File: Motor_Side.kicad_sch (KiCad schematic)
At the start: 30 parts, among them U2 TLV9301xDCK, U3 TLV9301xDCK, U4 TCMT1106, U5 TCMT1106

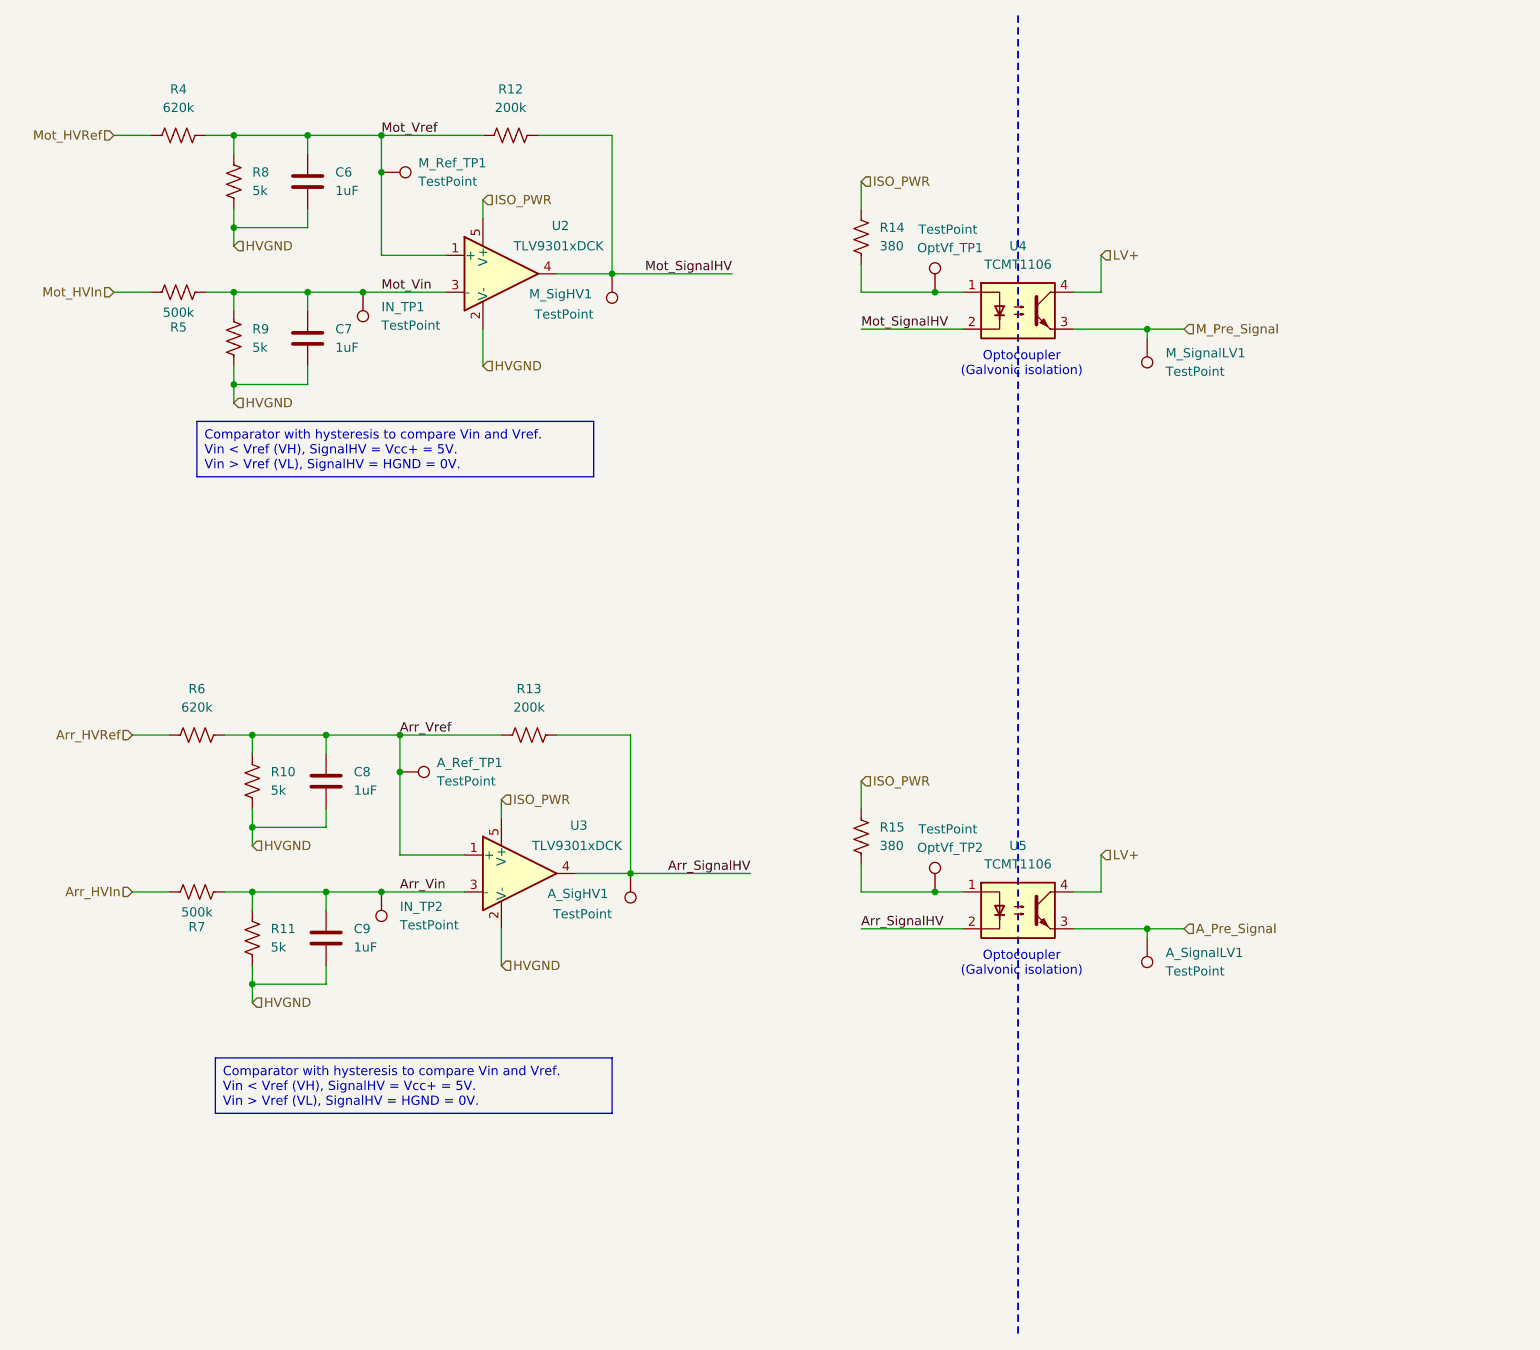
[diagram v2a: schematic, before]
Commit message: started on HV layout
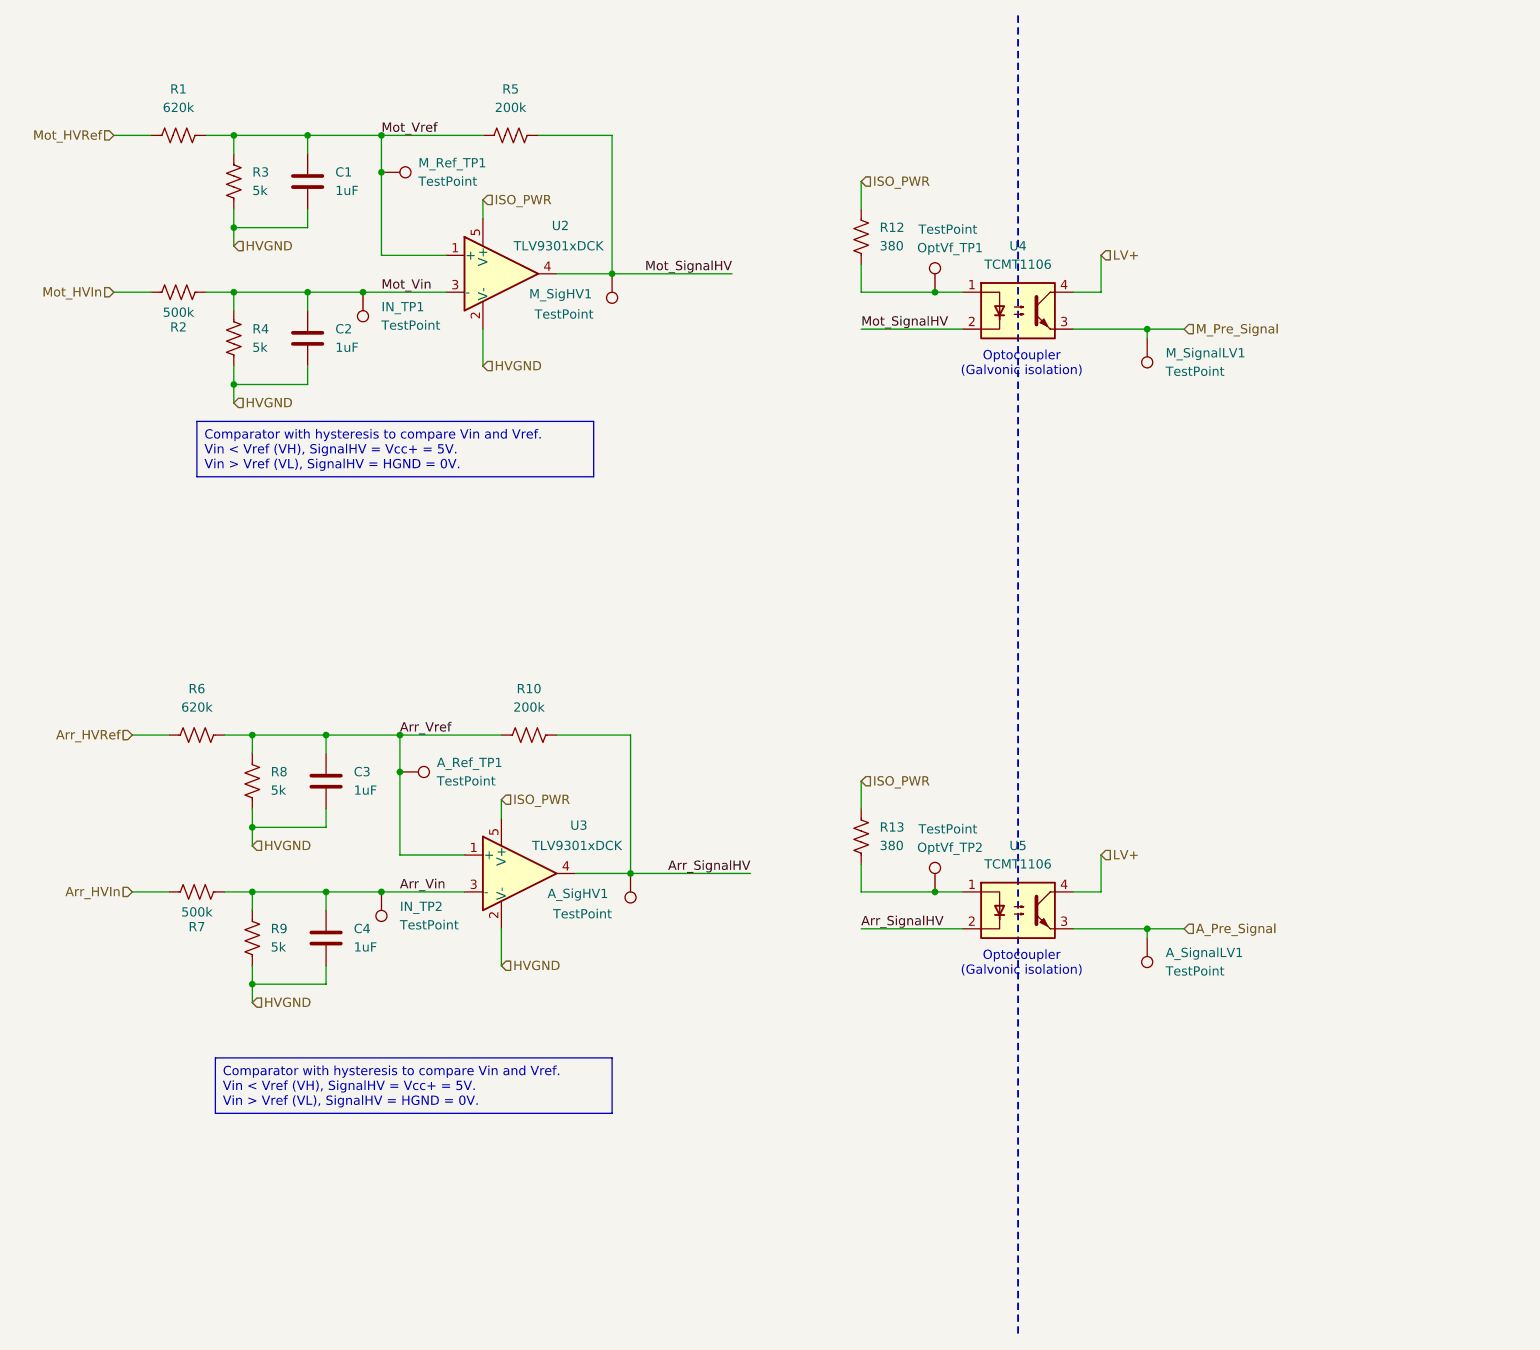
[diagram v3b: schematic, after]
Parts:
- renumbered C6 to C1, C7 to C2, C8 to C3, C9 to C4, R4 to R1, R13 to R10, R14 to R12, R15 to R13, R5 to R2, R8 to R3, R9 to R4, R12 to R5, R10 to R8, R11 to R9
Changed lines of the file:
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@@
 		(on_board yes)
 		(dnp no)
-		(property "Reference" "R5"
+		(property "Reference" "R2"
 			(at 48.26 56.896 90)
 			(effects
@@
 			(project "ActivePrecharge"
 				(path "/b9847a31-2b3b-47ca-9561-fab506416f6d/27dbb16c-0867-45c1-9eb8-11b8a424e215"
-					(reference "R5")
+					(reference "R2")
 					(unit 1)
 				)
@@
 		(dnp no)
 		(fields_autoplaced yes)
-		(property "Reference" "R13"
+		(property "Reference" "R10"
 			(at 96.52 106.68 90)
 			(effects
@@
 			(project "ActivePrecharge"
 				(path "/b9847a31-2b3b-47ca-9561-fab506416f6d/27dbb16c-0867-45c1-9eb8-11b8a424e215"
-					(reference "R13")
+					(reference "R10")
 					(unit 1)
 				)
@@
 		(dnp no)
 		(fields_autoplaced yes)
-		(property "Reference" "C9"
+		(property "Reference" "C4"
 			(at 72.39 139.6999 0)
 			(effects
@@
 			(project "ActivePrecharge"
 				(path "/b9847a31-2b3b-47ca-9561-fab506416f6d/27dbb16c-0867-45c1-9eb8-11b8a424e215"
-					(reference "C9")
+					(reference "C4")
 					(unit 1)
 				)
@@
 		(dnp no)
 		(fields_autoplaced yes)
-		(property "Reference" "R14"
+		(property "Reference" "R12"
 			(at 144.78 43.1799 0)
 			(effects
@@
 			(project "ActivePrecharge"
 				(path "/b9847a31-2b3b-47ca-9561-fab506416f6d/27dbb16c-0867-45c1-9eb8-11b8a424e215"
-					(reference "R14")
+					(reference "R12")
 					(unit 1)
 				)
@@
 		(dnp no)
 		(fields_autoplaced yes)
-		(property "Reference" "C6"
+		(property "Reference" "C1"
 			(at 69.85 35.5599 0)
 			(effects
@@
 			(project "ActivePrecharge"
 				(path "/b9847a31-2b3b-47ca-9561-fab506416f6d/27dbb16c-0867-45c1-9eb8-11b8a424e215"
-					(reference "C6")
+					(reference "C1")
 					(unit 1)
 				)
@@
 		(dnp no)
 		(fields_autoplaced yes)
-		(property "Reference" "C8"
+		(property "Reference" "C3"
 			(at 72.39 118.1099 0)
 			(effects
@@
 			(project "ActivePrecharge"
 				(path "/b9847a31-2b3b-47ca-9561-fab506416f6d/27dbb16c-0867-45c1-9eb8-11b8a424e215"
-					(reference "C8")
+					(reference "C3")
 					(unit 1)
 				)
@@
 		(dnp no)
 		(fields_autoplaced yes)
-		(property "Reference" "R15"
+		(property "Reference" "R13"
 			(at 144.78 125.7299 0)
 			(effects
@@
 			(project "ActivePrecharge"
 				(path "/b9847a31-2b3b-47ca-9561-fab506416f6d/27dbb16c-0867-45c1-9eb8-11b8a424e215"
-					(reference "R15")
+					(reference "R13")
 					(unit 1)
 				)
@@
 		(dnp no)
 		(fields_autoplaced yes)
-		(property "Reference" "R10"
+		(property "Reference" "R8"
 			(at 60.96 118.1099 0)
 			(effects
@@
 			(project "ActivePrecharge"
 				(path "/b9847a31-2b3b-47ca-9561-fab506416f6d/27dbb16c-0867-45c1-9eb8-11b8a424e215"
-					(reference "R10")
+					(reference "R8")
 					(unit 1)
 				)
@@
 		(dnp no)
 		(fields_autoplaced yes)
-		(property "Reference" "C7"
+		(property "Reference" "C2"
 			(at 69.85 57.1499 0)
 			(effects
@@
 			(project "ActivePrecharge"
 				(path "/b9847a31-2b3b-47ca-9561-fab506416f6d/27dbb16c-0867-45c1-9eb8-11b8a424e215"
-					(reference "C7")
+					(reference "C2")
 					(unit 1)
 				)
@@
 		(dnp no)
 		(fields_autoplaced yes)
-		(property "Reference" "R12"
+		(property "Reference" "R5"
 			(at 93.98 24.13 90)
 			(effects
@@
 			(project "ActivePrecharge"
 				(path "/b9847a31-2b3b-47ca-9561-fab506416f6d/27dbb16c-0867-45c1-9eb8-11b8a424e215"
-					(reference "R12")
+					(reference "R5")
 					(unit 1)
 				)
@@
 		(dnp no)
 		(fields_autoplaced yes)
-		(property "Reference" "R9"
+		(property "Reference" "R4"
 			(at 58.42 57.1499 0)
 			(effects
@@
 			(project "ActivePrecharge"
 				(path "/b9847a31-2b3b-47ca-9561-fab506416f6d/27dbb16c-0867-45c1-9eb8-11b8a424e215"
-					(reference "R9")
+					(reference "R4")
 					(unit 1)
 				)
@@
 		(dnp no)
 		(fields_autoplaced yes)
-		(property "Reference" "R4"
+		(property "Reference" "R1"
 			(at 48.26 24.13 90)
 			(effects
@@
 			(project "ActivePrecharge"
 				(path "/b9847a31-2b3b-47ca-9561-fab506416f6d/27dbb16c-0867-45c1-9eb8-11b8a424e215"
-					(reference "R4")
+					(reference "R1")
 					(unit 1)
 				)
@@
 		(dnp no)
 		(fields_autoplaced yes)
-		(property "Reference" "R8"
+		(property "Reference" "R3"
 			(at 58.42 35.5599 0)
 			(effects
@@
 			(project "ActivePrecharge"
 				(path "/b9847a31-2b3b-47ca-9561-fab506416f6d/27dbb16c-0867-45c1-9eb8-11b8a424e215"
-					(reference "R8")
+					(reference "R3")
 					(unit 1)
 				)
@@
 		(dnp no)
 		(fields_autoplaced yes)
-		(property "Reference" "R11"
+		(property "Reference" "R9"
 			(at 60.96 139.6999 0)
 			(effects
@@
 			(project "ActivePrecharge"
 				(path "/b9847a31-2b3b-47ca-9561-fab506416f6d/27dbb16c-0867-45c1-9eb8-11b8a424e215"
-					(reference "R11")
-					(unit 1)
-				)
+					(reference "R9")
+					(unit 1)
+				)

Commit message: fixed lakshay and ravi comments, renamed signals to be more readable, further worked on HV side layout
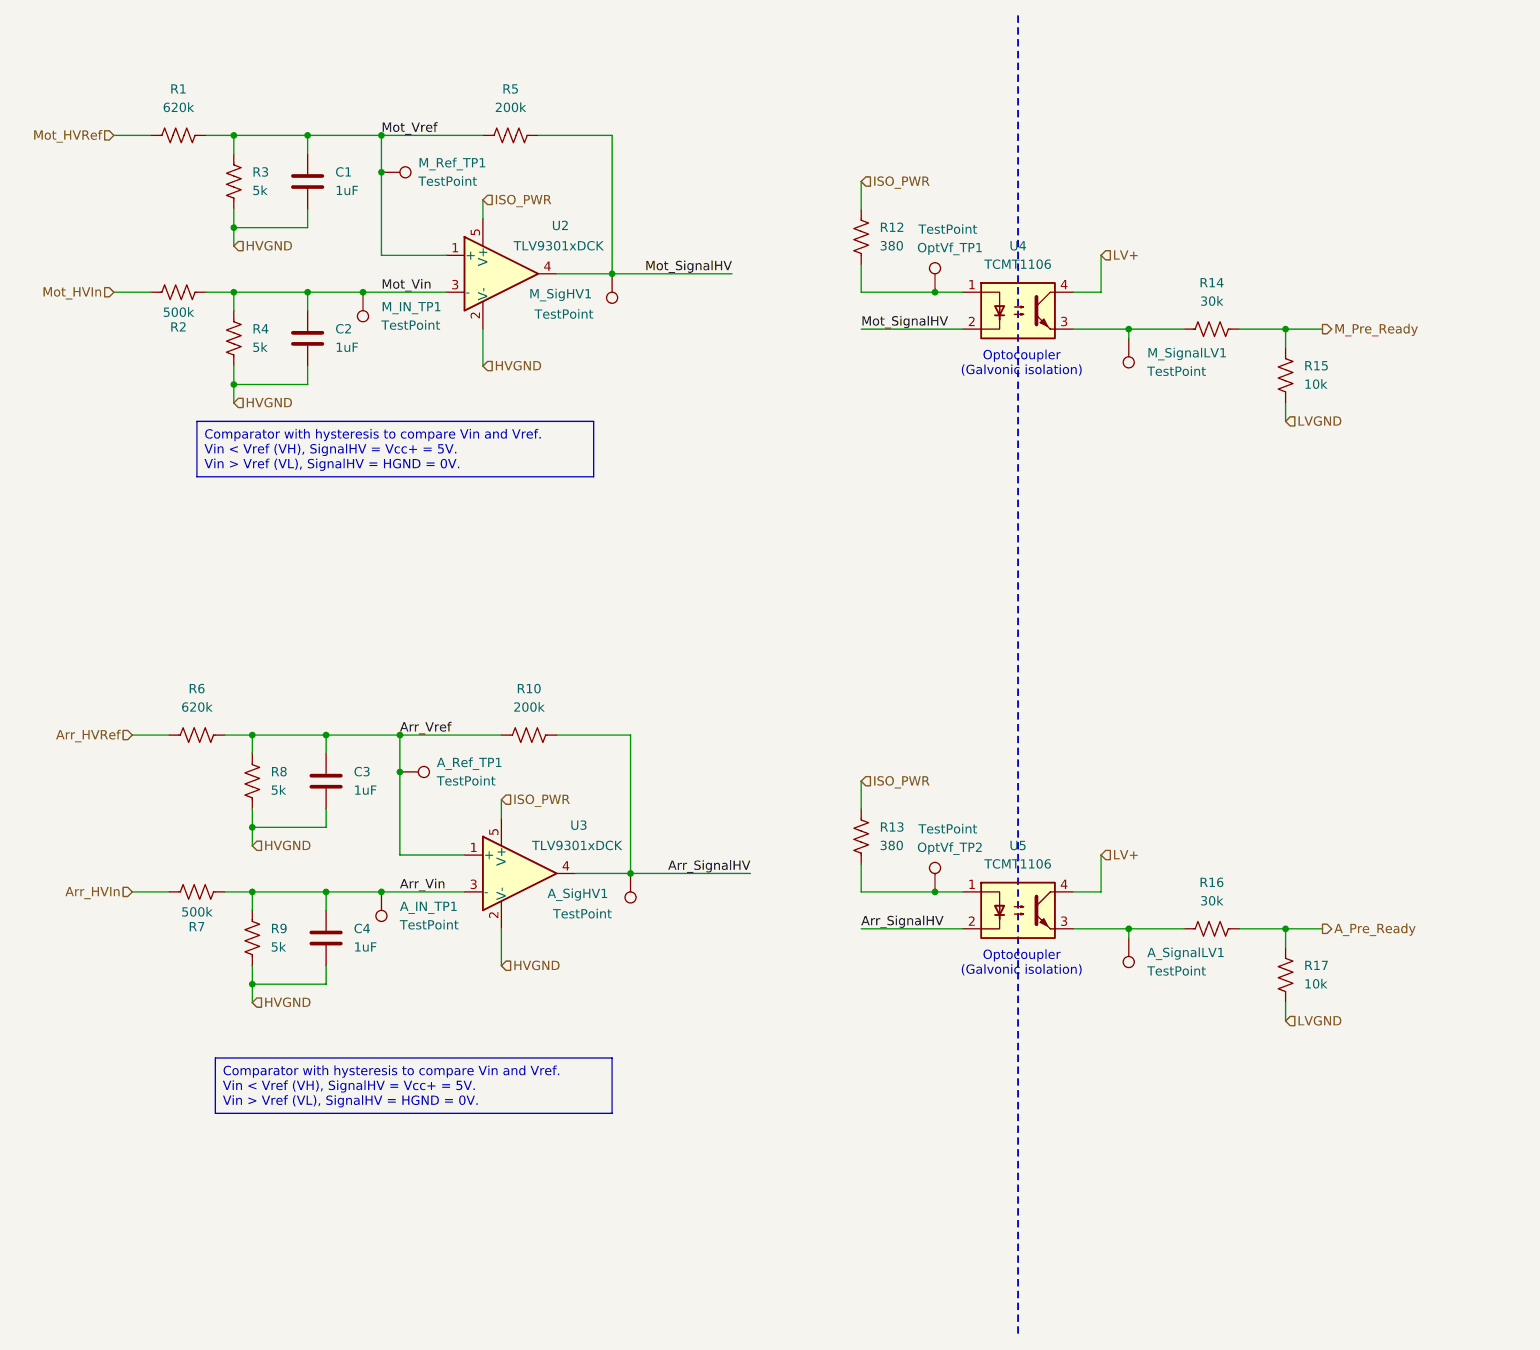
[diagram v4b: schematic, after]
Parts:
- added R14, R16: 30k, symbol Device:R_US
- added R15, R17: 10k, symbol Device:R_US
- renumbered IN_TP2 to A_IN_TP1, IN_TP1 to M_IN_TP1
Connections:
- net A_Pre_Signal: no longer names the net of A_SignalLV1.1, U5.3
- net A_Pre_Signal: now also R16.1
- net M_Pre_Signal: no longer names the net of M_SignalLV1.1, U4.3
- net M_Pre_Signal: now also R14.1
- new net A_Pre_Ready: R16.2, R17.1
- new net LVGND: R15.2, R17.2
- new net M_Pre_Ready: R14.2, R15.1
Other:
- moved on the sheet: M_SignalLV1

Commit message: end of workday, will work on more tonight
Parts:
- removed OptVf_TP1, OptVf_TP2: TestPoint, utsvt-special:TestPoint_HEX_3mmID, symbol Connector:TestPoint
- R14, R15, R16, R17: footprint (none) -> Resistor_SMD:R_0805_2012Metric
- renumbered A_SignalLV1 to A_Pre_Ready_TP1, M_SignalLV1 to M_Pre_Ready_TP1
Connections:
- net A_Pre_Ready: now also A_Pre_Ready_TP1.1
- net M_Pre_Ready: now also M_Pre_Ready_TP1.1
- net at R16.1, U5.3: no longer A_Pre_Ready_TP1.1
- net at R14.1, U4.3: no longer M_Pre_Ready_TP1.1
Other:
- moved on the sheet: A_Pre_Ready_TP1, M_Pre_Ready_TP1

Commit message: initial commit v2
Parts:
- added Q2, Q3: IRLML0030, Package_TO_SOT_SMD:SOT-23, symbol Transistor_FET:IRLML0030
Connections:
- net Arr_SignalHV: now also Q3.3 (D); no longer A_SigHV1.1, R10.1, U3.4
- net Arr_Vref: now also Q3.1 (G)
- net Mot_SignalHV: now also Q2.3 (D); no longer M_SigHV1.1, R5.1, U2.4
- net Mot_Vref: now also Q2.1 (G)
- new net: A_SigHV1.1, Q3.2 (S), R10.1, U3.4
- new net: M_SigHV1.1, Q2.2 (S), R5.1, U2.4
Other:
- moved on the sheet: A_IN_TP1, A_Pre_Ready_TP1, A_Ref_TP1, A_SigHV1, C1, C2, C3, C4, M_IN_TP1, M_Pre_Ready_TP1, M_Ref_TP1, M_SigHV1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
